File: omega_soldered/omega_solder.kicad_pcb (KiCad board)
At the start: 2 copper layers, 200.8 x 58.9 mm, 63 parts, among them SW1 SW_Push, U1 ProMicro

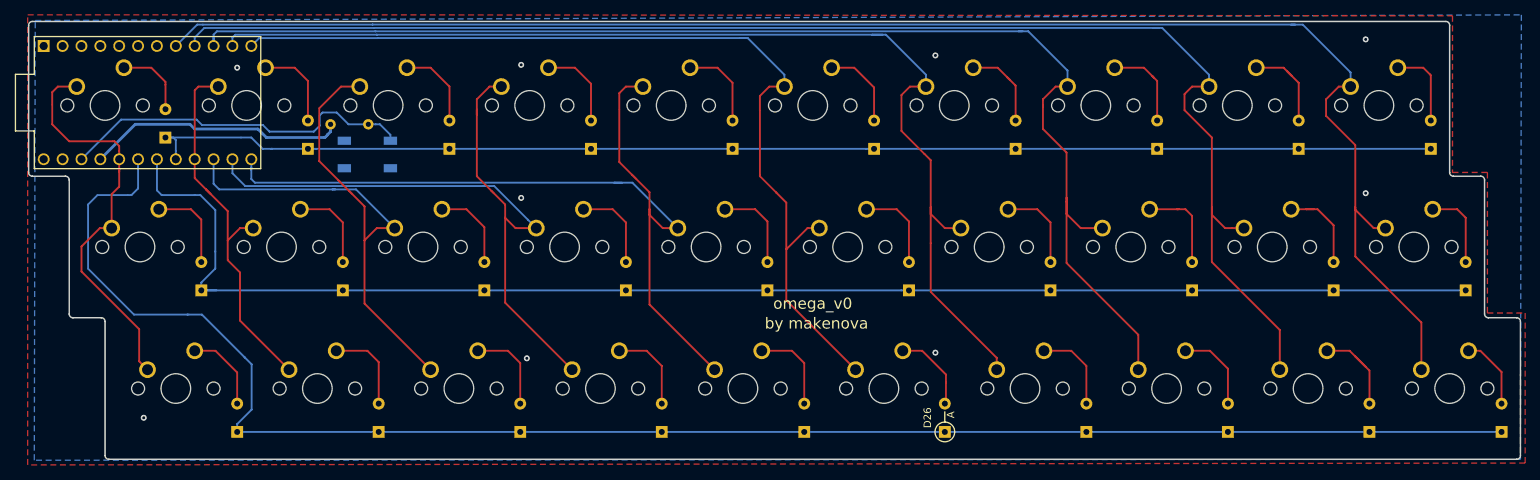
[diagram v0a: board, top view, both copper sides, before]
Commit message: add solder version
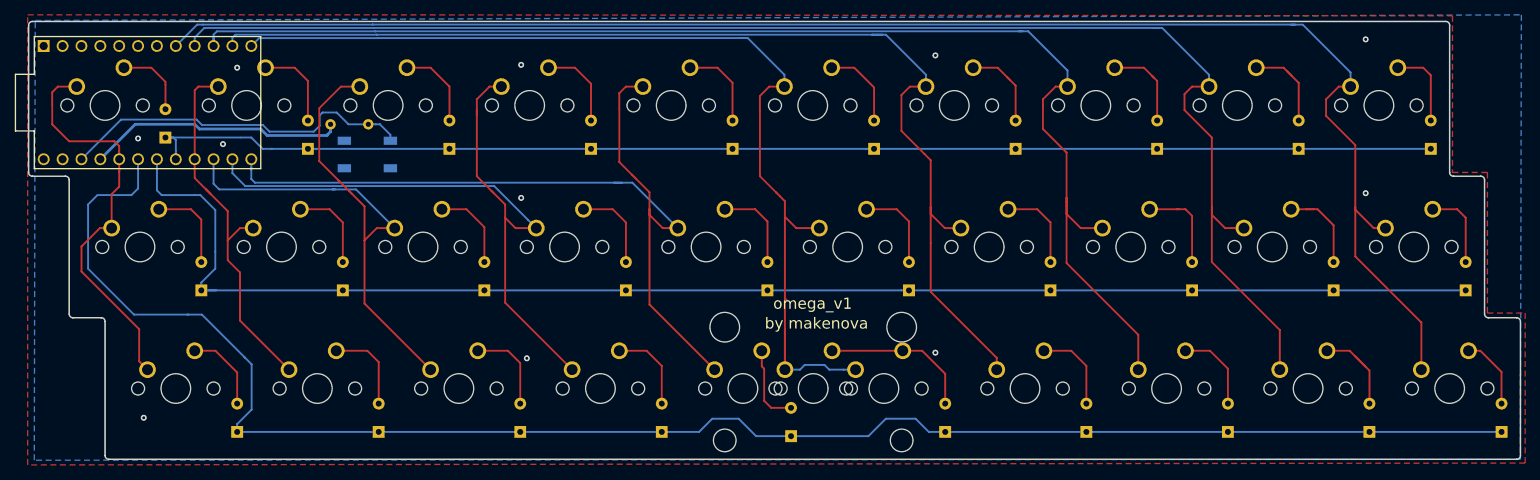
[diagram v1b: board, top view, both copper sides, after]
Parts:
- added MX31: MX-NoLED, MX_Only:MXOnly-2U-ReversedStabilizers-NoLED, F.Cu at (160.8, 89.0)
- D26: moved to B.Cu
- moved D25 1.87 mm to (157.9, 95.4)
- moved D26 0.05 mm to (178.6, 94.9)
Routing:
- net COL5: track 128.3 -> 139.6 mm
- net Net-(D26-Pad2): track 11.0 -> 20.5 mm
- net ROW2: track 228.1 -> 231.5 mm
- net Net-(D25-Pad2): track 11.9 -> 10.9 mm
- net GND: vias 9 -> 11
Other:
- board text added: "omega_v1"
- board text removed: "omega_v0"

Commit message: work
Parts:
- added H1: Hole, MountingHole:MountingHole_2.2mm_M2, F.Cu at (79.8, 60.7)
- added H2: Hole, MountingHole:MountingHole_2.2mm_M2, F.Cu at (232.2, 79.5)
- added H3: Hole, MountingHole:MountingHole_2.2mm_M2, F.Cu at (79.8, 79.5)
- added H4: Hole, MountingHole:MountingHole_2.2mm_M2, F.Cu at (232.2, 60.5)
- D1, D10, D11, D12, D13, D14, D15, D16, D17, D18, D19, D2, D20, D21, D22, D23, D24, D25, D26, D27, D28, D29, D3, D30, D4, D5, D6, D7, D8, D9: footprint Diode_THT:D_DO-35_SOD27_P3.81mm_Vertical_AnodeUp -> Keebio-Parts:Diode-Hybrid-Back; moved to F.Cu
- moved D30 4.01 mm to (254.3, 90.9), turned to 270 degrees
- moved D20 3.97 mm to (249.2, 71.9), turned to 270 degrees
- moved D17 3.94 mm to (192.7, 71.9), turned to 270 degrees
- moved D18 3.94 mm to (211.7, 71.9), turned to 270 degrees
- moved D19 3.94 mm to (230.8, 71.9), turned to 270 degrees
- moved D23 3.94 mm to (121.3, 90.9), turned to 270 degrees
- moved D21 3.94 mm to (83.2, 90.9), turned to 270 degrees
- moved D22 3.94 mm to (102.2, 90.9), turned to 270 degrees
- moved D24 3.94 mm to (140.3, 90.9), turned to 270 degrees
- moved D2 3.94 mm to (92.8, 52.8), turned to 270 degrees
- moved D10 3.89 mm to (244.6, 52.9), turned to 270 degrees
- moved D29 3.89 mm to (235.6, 91.0), turned to 270 degrees
- moved D11 3.88 mm to (78.4, 71.9), turned to 270 degrees
- moved D12 3.88 mm to (97.4, 71.9), turned to 270 degrees
- moved D13 3.88 mm to (116.5, 71.9), turned to 270 degrees
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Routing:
- net Net-(D25-Pad2): track 10.9 -> 19.1 mm
- net Net-(R1-Pad2): track 48.4 -> 54.3 mm, vias 0 -> 2
- net Net-(D29-Pad2): track 13.2 -> 8.02 mm
- net Net-(D19-Pad2): track 12.6 -> 7.53 mm
- net Net-(D18-Pad2): track 12.6 -> 7.53 mm
- net ROW2: track 231.5 -> 236.6 mm
- net Net-(D9-Pad2): track 12.5 -> 7.57 mm
- net Net-(D8-Pad2): track 12.1 -> 7.58 mm
- net Net-(D11-Pad2): track 12.0 -> 7.55 mm
- net Net-(D15-Pad2): track 11.9 -> 7.55 mm
- net Net-(D16-Pad2): track 11.9 -> 7.55 mm
- net Net-(D7-Pad2): track 11.9 -> 7.58 mm
- net Net-(D17-Pad2): track 11.8 -> 7.53 mm
- net Net-(D14-Pad2): track 11.8 -> 7.55 mm
- net Net-(D12-Pad2): track 11.8 -> 7.55 mm
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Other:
- board text added: "omega_v2"
- board text removed: "omega_v1"

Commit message: update soldered omega
flip pro micro footprint
shuffle mounting holes
make stl files to 3D print for testing
regenerate gerbers
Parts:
- removed R1: 10k, Resistor_THT:R_Axial_DIN0204_L3.6mm_D1.6mm_P5.08mm_Horizontal
- H1, H2, H3, H4: footprint MountingHole:MountingHole_2.2mm_M2 -> MountingHole:MountingHole_3.2mm_M3_ISO7380
- SW1: footprint random-keyboard-parts:SKQG-1155865 -> Button_Switch_SMD:SW_DIP_SPSTx01_Slide_Copal_CHS-01A_W5.08mm_P1.27mm_JPin
- U1: moved to F.Cu
- moved SW1 41.6 mm to (62.8, 40.6), turned to 180 degrees
- moved D1 2.10 mm to (75.8, 51.3)
- moved H1 1.40 mm to (79.8, 62.1)
- moved H2 0.26 mm to (232.1, 79.2)
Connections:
- U1 pad 10: COL7 -> COL2
- U1 pad 11: COL6 -> COL3
- U1 pad 12: COL5 -> COL4
- U1 pad 13: COL4 -> COL5
- U1 pad 14: COL3 -> COL6
- U1 pad 15: COL2 -> COL7
- U1 pad 16: COL1 -> COL8
- U1 pad 17: ROW0 -> COL9
- U1 pad 18: ROW1 -> Net-(U1-Pad18)
- U1 pad 19: ROW2 -> Net-(U1-Pad19)
- U1 pad 20: COL0 -> Net-(U1-Pad20)
- U1 pad 5: Net-(U1-Pad5) -> COL0
- U1 pad 6: Net-(U1-Pad6) -> ROW2
- U1 pad 7: Net-(U1-Pad7) -> ROW1
- U1 pad 8: COL9 -> ROW0
- U1 pad 9: COL8 -> COL1
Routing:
- net Net-(SW1-Pad1): track 54.3 -> 2.86 mm, vias 2 -> 0
- net +5V: track 35.1 -> 0.00 mm
- net ROW1: track 194.9 -> 212.4 mm
- net COL1: track 51.8 -> 65.9 mm
- net ROW0: track 176.1 -> 172.4 mm
- net GND: track 0.00 -> 2.89 mm, vias 11 -> 14
- net Net-(D1-Pad2): track 6.64 -> 8.99 mm
- net COL4: track 114.2 -> 112.4 mm
- net COL2: track 81.2 -> 79.5 mm
- net COL7: track 172.5 -> 171.1 mm
- net COL8: track 193.6 -> 192.6 mm
- net COL6: track 149.2 -> 148.7 mm
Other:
- board text added: "omega_v2.1 by makenova"
- board text removed: "by makenova"
- board text removed: "omega_v2"

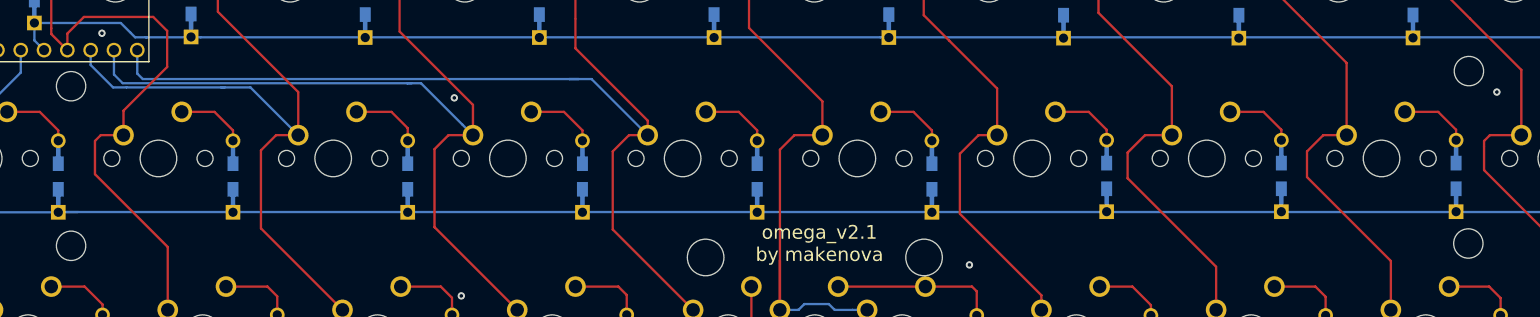
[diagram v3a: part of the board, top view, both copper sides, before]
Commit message: update soldered omega
increase stanoff hole size through the pcb
update stl files and step files
shuffle file locations
regenerate gerbers
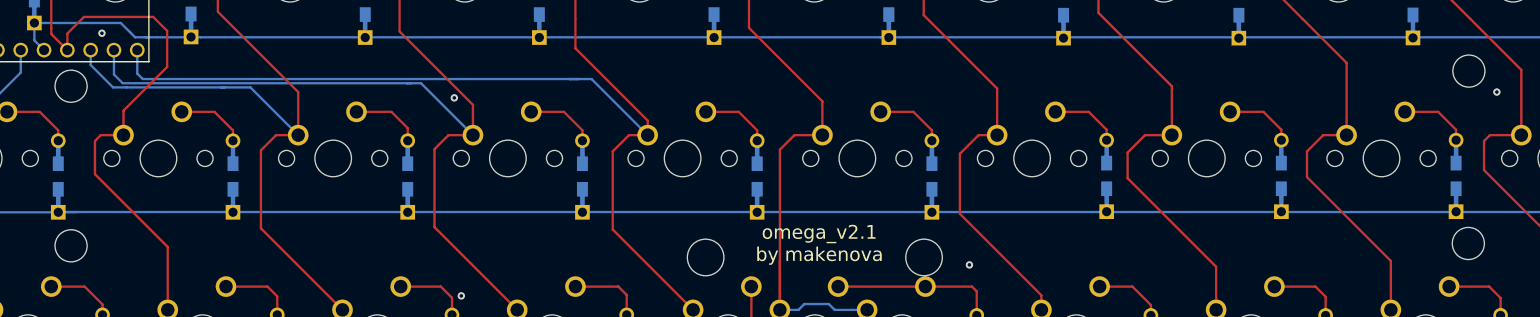
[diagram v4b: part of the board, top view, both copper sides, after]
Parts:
- H1, H2, H3, H4: footprint MountingHole:MountingHole_3.2mm_M3_ISO7380 -> MountingHole:MountingHole_3.5mm

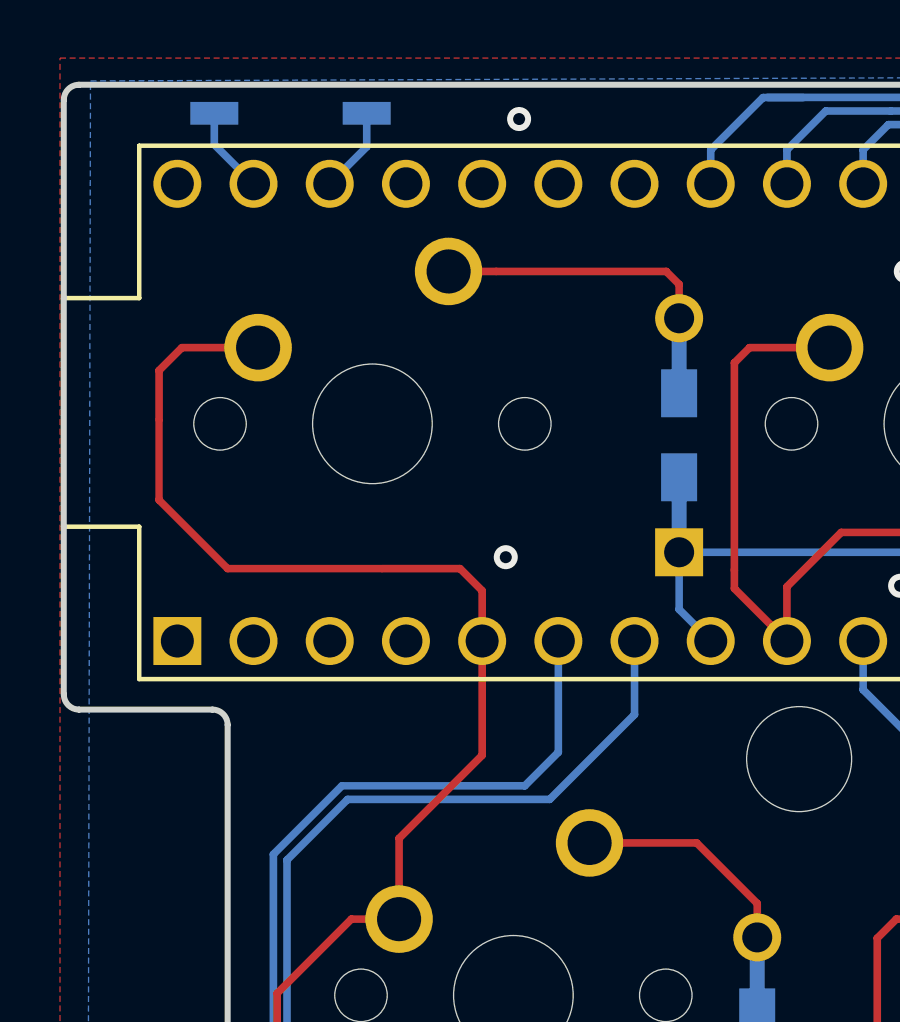
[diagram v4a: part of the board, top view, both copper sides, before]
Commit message: do not use series pins on omega soldered
regenerage gerber files for omega soldered and omega 4
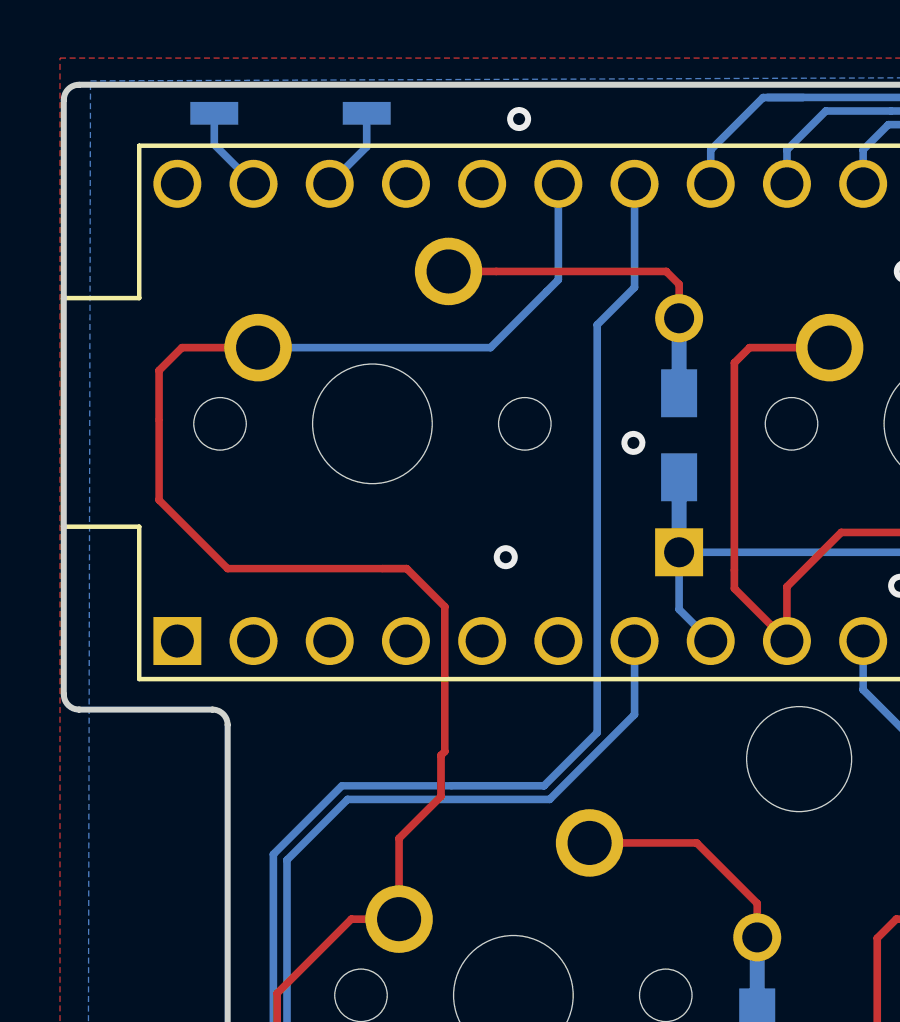
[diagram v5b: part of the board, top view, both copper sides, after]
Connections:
- U1 pad 18: Net-(U1-Pad18) -> ROW2
- U1 pad 19: Net-(U1-Pad19) -> COL0
- U1 pad 5: COL0 -> Net-(U1-Pad5)
- U1 pad 6: ROW2 -> Net-(U1-Pad6)
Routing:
- net ROW2: track 236.5 -> 253.1 mm
- net COL0: track 57.4 -> 69.5 mm
- net GND: vias 14 -> 15
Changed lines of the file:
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@@
     (thickness 1.6)
     (drawings 25)
-    (tracks 373)
+    (tracks 381)
     (zones 0)
     (modules 67)
@@
   (net 48 "Net-(D30-Pad2)")
   (net 49 "Net-(U1-Pad20)")
-  (net 50 "Net-(U1-Pad19)")
-  (net 51 "Net-(U1-Pad18)")
-  (net 52 "Net-(SW1-Pad1)")
+  (net 50 "Net-(SW1-Pad1)")
+  (net 51 "Net-(U1-Pad6)")
+  (net 52 "Net-(U1-Pad5)")
   (net_class Default "This is the default net class."
     (clearance 0.2)
@@
     (add_net "Net-(SW1-Pad1)")
     (add_net "Net-(U1-Pad1)")
-    (add_net "Net-(U1-Pad18)")
-    (add_net "Net-(U1-Pad19)")
     (add_net "Net-(U1-Pad2)")
     (add_net "Net-(U1-Pad20)")
     (add_net "Net-(U1-Pad24)")
+    (add_net "Net-(U1-Pad5)")
+    (add_net "Net-(U1-Pad6)")
     (add_net ROW0)
     (add_net ROW1)
@@
       (net 1 GND))
     (pad 1 smd rect (at -2.54 0 180) (size 1.6 0.76) (layers B.Cu B.Paste B.Mask)
-      (net 52 "Net-(SW1-Pad1)"))
+      (net 50 "Net-(SW1-Pad1)"))
     (model ${KISYS3DMOD}/Button_Switch_SMD.3dshapes/SW_DIP_SPSTx01_Slide_Copal_CHS-01A_W5.08mm_P1.27mm_JPin.wrl
       (at (xyz 0 0 0))
@@
       (net 1 GND))
     (pad 22 thru_hole circle (at -8.89 -7.62) (size 1.6 1.6) (drill 1.1) (layers *.Cu *.Mask F.SilkS)
-      (net 52 "Net-(SW1-Pad1)"))
+      (net 50 "Net-(SW1-Pad1)"))
     (pad 21 thru_hole circle (at -6.35 -7.62) (size 1.6 1.6) (drill 1.1) (layers *.Cu *.Mask F.SilkS)
       (net 2 +5V))
@@
       (net 49 "Net-(U1-Pad20)"))
     (pad 19 thru_hole circle (at -1.27 -7.62) (size 1.6 1.6) (drill 1.1) (layers *.Cu *.Mask F.SilkS)
-      (net 50 "Net-(U1-Pad19)"))
+      (net 35 COL0))
     (pad 18 thru_hole circle (at 1.27 -7.62) (size 1.6 1.6) (drill 1.1) (layers *.Cu *.Mask F.SilkS)
-      (net 51 "Net-(U1-Pad18)"))
+      (net 26 ROW2))
     (pad 17 thru_hole circle (at 3.81 -7.62) (size 1.6 1.6) (drill 1.1) (layers *.Cu *.Mask F.SilkS)
       (net 44 COL9))
@@
       (net 15 ROW1))
     (pad 6 thru_hole circle (at -1.27 7.62) (size 1.6 1.6) (drill 1.1) (layers *.Cu *.Mask F.SilkS)
-      (net 26 ROW2))
+      (net 51 "Net-(U1-Pad6)"))
     (pad 5 thru_hole circle (at -3.81 7.62) (size 1.6 1.6) (drill 1.1) (layers *.Cu *.Mask F.SilkS)
-      (net 35 COL0))
+      (net 52 "Net-(U1-Pad5)"))
     (pad 4 thru_hole circle (at -6.35 7.62) (size 1.6 1.6) (drill 1.1) (layers *.Cu *.Mask F.SilkS)
       (net 1 GND))
@@
   (segment (start 60.2615 40.5765) (end 60.2615 41.6179) (width 0.254) (layer B.Cu) (net 1))
   (via (at 70.4215 40.767) (size 0.8) (drill 0.4) (layers F.Cu B.Cu) (net 1))
+  (via (at 74.2315 51.562) (size 0.8) (drill 0.4) (layers F.Cu B.Cu) (net 1))
   (segment (start 69.66299 45.847) (end 68.072 45.847) (width 0.254) (layer F.Cu) (net 3))
   (segment (start 75.32587 45.847) (end 69.66299 45.847) (width 0.254) (layer F.Cu) (net 3))
@@
   (segment (start 145.4785 94.869) (end 147.2565 93.091) (width 0.254) (layer B.Cu) (net 26))
   (segment (start 83.312 93.815) (end 83.312 94.869) (width 0.254) (layer B.Cu) (net 26))
-  (segment (start 68.1736 62.992) (end 70.612 62.992) (width 0.254) (layer B.Cu) (net 26))
   (segment (start 68.1736 62.992) (end 64.516 62.992) (width 0.25) (layer B.Cu) (net 26))
-  (segment (start 70.612 62.992) (end 71.7296 61.8744) (width 0.254) (layer B.Cu) (net 26))
-  (segment (start 71.7296 61.8744) (end 71.7296 58.166) (width 0.254) (layer B.Cu) (net 26))
   (segment (start 176.403 94.869) (end 178.6128 94.869) (width 0.254) (layer B.Cu) (net 26))
   (segment (start 174.625 93.091) (end 176.403 94.869) (width 0.254) (layer B.Cu) (net 26))
@@
   (segment (start 62.23 65.278) (end 64.516 62.992) (width 0.254) (layer B.Cu) (net 26))
   (segment (start 62.23 72.8345) (end 62.23 65.278) (width 0.254) (layer B.Cu) (net 26))
+  (segment (start 71.252634 62.992) (end 68.1736 62.992) (width 0.254) (layer B.Cu) (net 26))
+  (segment (start 73.025 61.219634) (end 71.252634 62.992) (width 0.254) (layer B.Cu) (net 26))
+  (segment (start 74.2696 46.3804) (end 73.025 47.625) (width 0.254) (layer B.Cu) (net 26))
+  (segment (start 73.025 47.625) (end 73.025 61.219634) (width 0.254) (layer B.Cu) (net 26))
+  (segment (start 74.2696 42.926) (end 74.2696 46.3804) (width 0.254) (layer B.Cu) (net 26))
   (segment (start 96.647 83.947) (end 101.1682 83.947) (width 0.254) (layer F.Cu) (net 27))
   (segment (start 102.235 85.0138) (end 101.1682 83.947) (width 0.254) (layer F.Cu) (net 27))
@@
   (segment (start 62.357 73.279) (end 62.357 69.91001) (width 0.254) (layer F.Cu) (net 35))
   (segment (start 60.706 55.753) (end 65.8622 55.753) (width 0.25) (layer F.Cu) (net 35))
-  (segment (start 65.8622 55.753) (end 68.453 55.753) (width 0.254) (layer F.Cu) (net 35))
-  (segment (start 68.453 55.753) (end 69.1896 56.4896) (width 0.254) (layer F.Cu) (net 35))
-  (segment (start 69.1896 56.4896) (end 69.1896 58.166) (width 0.254) (layer F.Cu) (net 35))
-  (segment (start 69.1896 61.976) (end 66.421 64.7446) (width 0.254) (layer F.Cu) (net 35))
-  (segment (start 69.1896 58.166) (end 69.1896 61.976) (width 0.254) (layer F.Cu) (net 35))
+  (segment (start 67.945 57.023) (end 66.675 55.753) (width 0.254) (layer F.Cu) (net 35))
+  (segment (start 67.945 61.849) (end 67.945 57.023) (width 0.254) (layer F.Cu) (net 35))
+  (segment (start 67.818 63.3476) (end 67.818 61.976) (width 0.254) (layer F.Cu) (net 35))
   (segment (start 66.421 67.437) (end 66.421 64.7446) (width 0.254) (layer F.Cu) (net 35))
+  (segment (start 67.818 61.976) (end 67.945 61.849) (width 0.254) (layer F.Cu) (net 35))
+  (segment (start 65.8622 55.753) (end 66.675 55.753) (width 0.254) (layer F.Cu) (net 35))
+  (segment (start 66.421 64.7446) (end 67.818 63.3476) (width 0.254) (layer F.Cu) (net 35))
+  (segment (start 61.722 48.387) (end 69.469 48.387) (width 0.254) (layer B.Cu) (net 35))
+  (segment (start 71.7296 46.1264) (end 71.34225 46.51375) (width 0.254) (layer B.Cu) (net 35))
+  (segment (start 71.7296 42.926) (end 71.7296 46.1264) (width 0.254) (layer B.Cu) (net 35))
+  (segment (start 69.469 48.387) (end 71.34225 46.51375) (width 0.254) (layer B.Cu) (net 35))
   (segment (start 78.105 48.387) (end 80.772 48.387) (width 0.254) (layer F.Cu) (net 36))
   (segment (start 77.597 48.895) (end 78.105 48.387) (width 0.254) (layer F.Cu) (net 36))
@@
   (segment (start 254.254 84.8868) (end 254.254 87.032) (width 0.254) (layer F.Cu) (net 48))
   (segment (start 253.3142 83.947) (end 254.254 84.8868) (width 0.254) (layer F.Cu) (net 48))
-  (segment (start 65.3415 41.6941) (end 65.3415 40.5765) (width 0.254) (layer B.Cu) (net 52))
-  (segment (start 64.1096 42.926) (end 65.3415 41.6941) (width 0.254) (layer B.Cu) (net 52))
+  (segment (start 65.3415 41.6941) (end 65.3415 40.5765) (width 0.254) (layer B.Cu) (net 50))
+  (segment (start 64.1096 42.926) (end 65.3415 41.6941) (width 0.254) (layer B.Cu) (net 50))
   (zone (net 1) (net_name GND) (layer B.Cu) (hatch edge 0.508)
     (connect_pads (clearance 0.508))
